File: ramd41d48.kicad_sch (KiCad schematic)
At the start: 14 parts, among them U23 SN74ALS253N (КР1533КП12), U24 SN74ALS253N (КР1533КП12), U26 SN74ALS253N (КР1533КП12), U27 SN74ALS253N (КР1533КП12), U41 2118 (КР565РУ6), U42 2118 (КР565РУ6), U43 2118 (КР565РУ6), U44 2118 (КР565РУ6), U45 2118 (КР565РУ6), U46 2118 (КР565РУ6)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

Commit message: March 22nd - 3rd edition
List 3 is complete
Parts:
- gave numbers to parts that had none: 1
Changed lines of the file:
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@@
   (symbol (lib_id "Jumper:Jumper_2_Open") (at 38.1 134.62 0) (unit 1)
     (in_bom yes) (on_board yes) (fields_autoplaced)
-    (property "Reference" "JP?" (id 0) (at 38.1 128.27 0))
+    (property "Reference" "JP3" (id 0) (at 38.1 128.27 0))
     (property "Value" "Jumper_2_Open" (id 1) (at 38.1 130.81 0))
     (property "Footprint" "Connector_PinHeader_2.54mm:PinHeader_1x02_P2.54mm_Vertical" (id 2) (at 38.1 134.62 0)
@@
   )
   (symbol (lib_id "Device:R") (at 38.1 127 90) (unit 1)
-    (in_bom yes) (on_board yes) (fields_autoplaced)
-    (property "Reference" "R14" (id 0) (at 38.1 120.65 90))
-    (property "Value" "10K" (id 1) (at 38.1 123.19 90))
+    (in_bom yes) (on_board yes)
+    (property "Reference" "R14" (id 0) (at 38.1 124.46 90))
+    (property "Value" "10K" (id 1) (at 38.1 127 90))
     (property "Footprint" "" (id 2) (at 38.1 128.778 90)
       (effects (font (size 1.27 1.27)) hide)

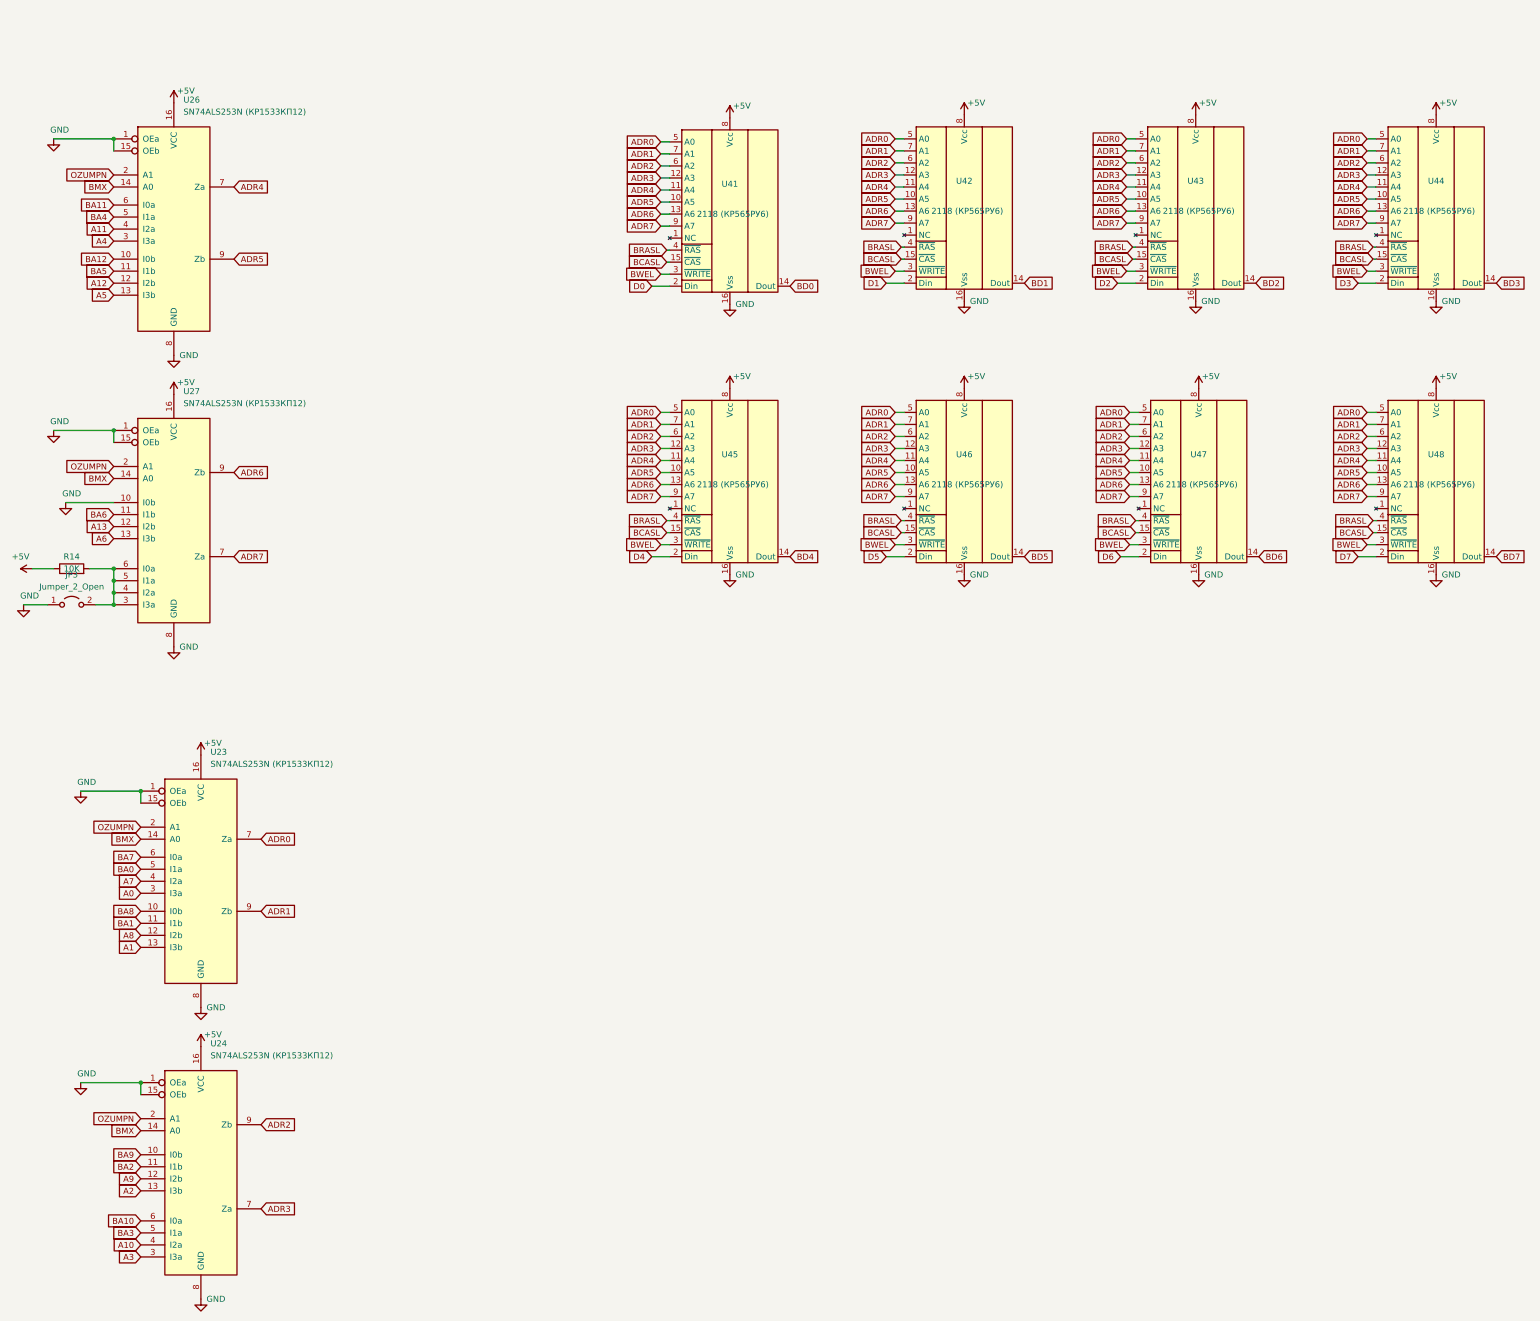
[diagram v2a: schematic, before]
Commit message: March 23rd First pre-alpha
First time ZERO errors and 93 warnings. Schematics are done, now to deal with warnings and footprints.
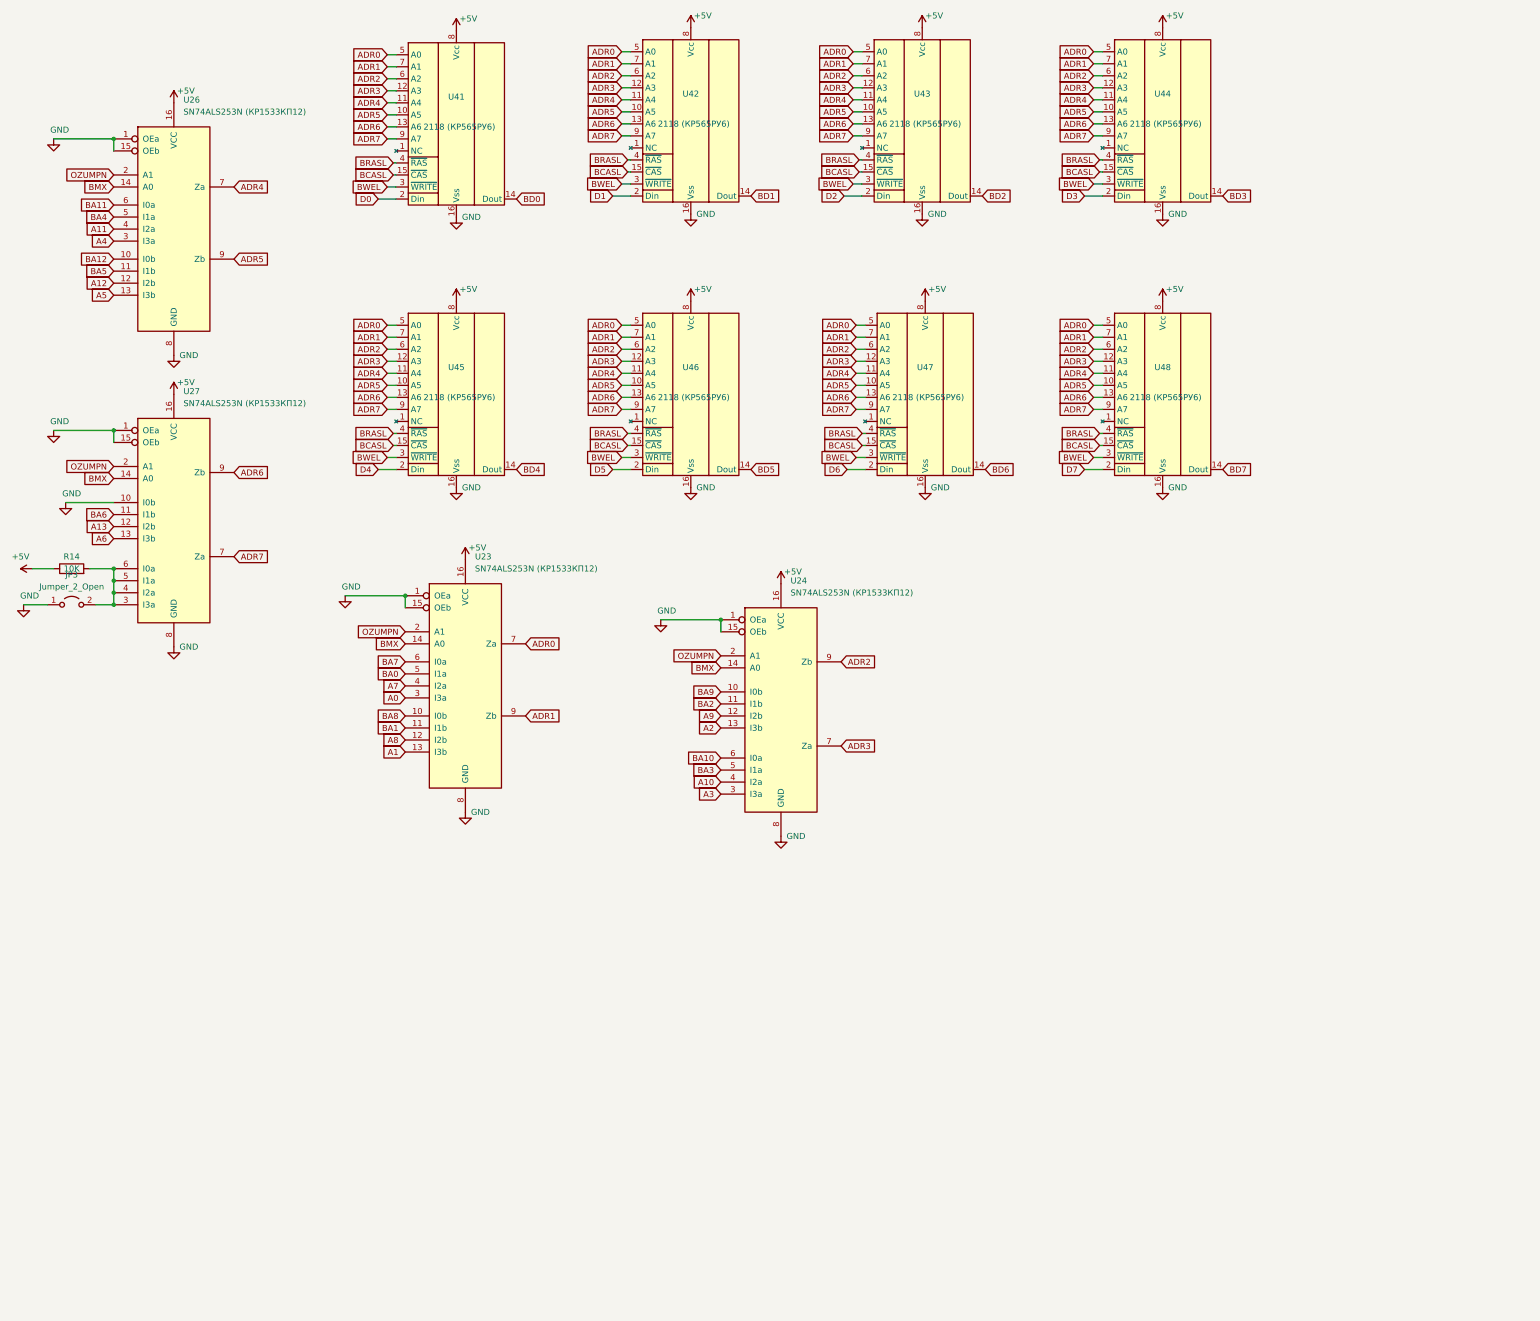
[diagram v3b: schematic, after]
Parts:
- R14: footprint (none) -> Resistor_THT:R_Axial_DIN0207_L6.3mm_D2.5mm_P10.16mm_Horizontal
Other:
- moved on the sheet: U23, U24, U41, U42, U43, U44, U45, U46, U47, U48

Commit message: March 24th Second Update
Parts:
- U23: symbol 74xx:74LS253 -> w_connectors:SN74ALS253N_(КР1533КП12)_U23
- U24: symbol 74xx:74LS253 -> w_connectors:SN74ALS253N_(КР1533КП12)_U24
- U26: symbol 74xx:74LS253 -> w_connectors:SN74ALS253N_(КР1533КП12)_U26
- U27: symbol 74xx:74LS253 -> w_connectors:SN74ALS253N_(КР1533КП12)_U27
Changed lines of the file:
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@@
     (pin "1")
   )
-  (symbol (lib_id "74xx:74LS253") (at 187.96 155.575 0) (unit 1)
+  (symbol (lib_id "w_connectors:SN74ALS253N_(КР1533КП12)_U24") (at 187.96 155.575 0) (unit 1)
     (in_bom yes) (on_board yes) (fields_autoplaced)
     (property "Reference" "U24" (id 0) (at 189.9794 129.54 0)
@@
     (pin "1")
   )
-  (symbol (lib_name "74LS253_1") (lib_id "74xx:74LS253") (at 59.69 53.975 0) (unit 1)
+  (symbol (lib_id "w_connectors:SN74ALS253N_(КР1533КП12)_U26") (at 59.69 53.975 0) (unit 1)
     (in_bom yes) (on_board yes) (fields_autoplaced)
     (property "Reference" "U26" (id 0) (at 61.7094 27.94 0)
@@
     (pin "1")
   )
-  (symbol (lib_name "74LS253_1") (lib_id "74xx:74LS253") (at 121.285 150.495 0) (unit 1)
+  (symbol (lib_id "w_connectors:SN74ALS253N_(КР1533КП12)_U23") (at 121.285 150.495 0) (unit 1)
     (in_bom yes) (on_board yes) (fields_autoplaced)
     (property "Reference" "U23" (id 0) (at 123.3044 124.46 0)
@@
     (pin "9")
   )
-  (symbol (lib_id "74xx:74LS253") (at 59.69 115.57 0) (unit 1)
+  (symbol (lib_id "w_connectors:SN74ALS253N_(КР1533КП12)_U27") (at 59.69 115.57 0) (unit 1)
     (in_bom yes) (on_board yes) (fields_autoplaced)
     (property "Reference" "U27" (id 0) (at 61.7094 89.535 0)

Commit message: March 26th update
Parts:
- U23, U24, U26, U27, U41, U42, U43, U44, U45, U46, U47, U48: footprint Package_DIP:DIP-16_W7.62mm_Socket_LongPads -> Package_DIP:DIP-16_W7.62mm_Socket
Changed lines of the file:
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@@
     (property "Reference" "U48" (id 0) (at 268.605 84.455 0))
     (property "Value" "2118 (КР565РУ6)" (id 1) (at 269.24 90.805 0))
-    (property "Footprint" "Package_DIP:DIP-16_W7.62mm_Socket_LongPads" (id 2) (at 255.905 75.565 0)
+    (property "Footprint" "Package_DIP:DIP-16_W7.62mm_Socket" (id 2) (at 255.905 75.565 0)
       (effects (font (size 1.27 1.27)) hide)
     )
@@
     (property "Reference" "U42" (id 0) (at 168.91 26.67 0))
     (property "Value" "2118 (КР565РУ6)" (id 1) (at 169.545 33.02 0))
-    (property "Footprint" "Package_DIP:DIP-16_W7.62mm_Socket_LongPads" (id 2) (at 156.21 17.78 0)
+    (property "Footprint" "Package_DIP:DIP-16_W7.62mm_Socket" (id 2) (at 156.21 17.78 0)
       (effects (font (size 1.27 1.27)) hide)
     )
@@
     (property "Reference" "U44" (id 0) (at 268.605 26.67 0))
     (property "Value" "2118 (КР565РУ6)" (id 1) (at 269.24 33.02 0))
-    (property "Footprint" "Package_DIP:DIP-16_W7.62mm_Socket_LongPads" (id 2) (at 255.905 17.78 0)
+    (property "Footprint" "Package_DIP:DIP-16_W7.62mm_Socket" (id 2) (at 255.905 17.78 0)
       (effects (font (size 1.27 1.27)) hide)
     )
@@
       (effects (font (size 1.27 1.27)) (justify left))
     )
-    (property "Footprint" "Package_DIP:DIP-16_W7.62mm_Socket_LongPads" (id 2) (at 186.69 159.385 0)
+    (property "Footprint" "Package_DIP:DIP-16_W7.62mm_Socket" (id 2) (at 186.69 159.385 0)
       (effects (font (size 1.27 1.27)) hide)
     )
@@
     (property "Reference" "U45" (id 0) (at 119.38 84.455 0))
     (property "Value" "2118 (КР565РУ6)" (id 1) (at 120.015 90.805 0))
-    (property "Footprint" "Package_DIP:DIP-16_W7.62mm_Socket_LongPads" (id 2) (at 106.68 75.565 0)
+    (property "Footprint" "Package_DIP:DIP-16_W7.62mm_Socket" (id 2) (at 106.68 75.565 0)
       (effects (font (size 1.27 1.27)) hide)
     )
@@
     (property "Reference" "U47" (id 0) (at 218.44 84.455 0))
     (property "Value" "2118 (КР565РУ6)" (id 1) (at 219.075 90.805 0))
-    (property "Footprint" "Package_DIP:DIP-16_W7.62mm_Socket_LongPads" (id 2) (at 205.74 75.565 0)
+    (property "Footprint" "Package_DIP:DIP-16_W7.62mm_Socket" (id 2) (at 205.74 75.565 0)
       (effects (font (size 1.27 1.27)) hide)
     )
@@
       (effects (font (size 1.27 1.27)) (justify left))
     )
-    (property "Footprint" "Package_DIP:DIP-16_W7.62mm_Socket_LongPads" (id 2) (at 59.69 53.975 0)
+    (property "Footprint" "Package_DIP:DIP-16_W7.62mm_Socket" (id 2) (at 59.69 53.975 0)
       (effects (font (size 1.27 1.27)) hide)
     )
@@
       (effects (font (size 1.27 1.27)) (justify left))
     )
-    (property "Footprint" "Package_DIP:DIP-16_W7.62mm_Socket_LongPads" (id 2) (at 121.285 150.495 0)
+    (property "Footprint" "Package_DIP:DIP-16_W7.62mm_Socket" (id 2) (at 121.285 150.495 0)
       (effects (font (size 1.27 1.27)) hide)
     )
@@
     (property "Reference" "U41" (id 0) (at 119.38 27.305 0))
     (property "Value" "2118 (КР565РУ6)" (id 1) (at 120.015 33.655 0))
-    (property "Footprint" "Package_DIP:DIP-16_W7.62mm_Socket_LongPads" (id 2) (at 106.68 18.415 0)
+    (property "Footprint" "Package_DIP:DIP-16_W7.62mm_Socket" (id 2) (at 106.68 18.415 0)
       (effects (font (size 1.27 1.27)) hide)
     )
@@
     (property "Reference" "U46" (id 0) (at 168.91 84.455 0))
     (property "Value" "2118 (КР565РУ6)" (id 1) (at 169.545 90.805 0))
-    (property "Footprint" "Package_DIP:DIP-16_W7.62mm_Socket_LongPads" (id 2) (at 156.21 75.565 0)
+    (property "Footprint" "Package_DIP:DIP-16_W7.62mm_Socket" (id 2) (at 156.21 75.565 0)
       (effects (font (size 1.27 1.27)) hide)
     )
@@
       (effects (font (size 1.27 1.27)) (justify left))
     )
-    (property "Footprint" "Package_DIP:DIP-16_W7.62mm_Socket_LongPads" (id 2) (at 58.42 119.38 0)
+    (property "Footprint" "Package_DIP:DIP-16_W7.62mm_Socket" (id 2) (at 58.42 119.38 0)
       (effects (font (size 1.27 1.27)) hide)
     )
@@
     (property "Reference" "U43" (id 0) (at 217.805 26.67 0))
     (property "Value" "2118 (КР565РУ6)" (id 1) (at 218.44 33.02 0))
-    (property "Footprint" "Package_DIP:DIP-16_W7.62mm_Socket_LongPads" (id 2) (at 205.105 17.78 0)
-      (effects (font (size 1.27 1.27)) hide)
-    )
+    (property "Footprint" "Package_DIP:DIP-16_W7.62mm_Socket" (id 2) (at 205.105 17.78 0)
+      (effects (font (size 1.27 1.27)) hide)
+    )
